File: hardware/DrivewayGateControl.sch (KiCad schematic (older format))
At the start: 50 parts, among them J1 serial_header, J2 magnetometer, J3 power, J4 Motor_Connects, J5 gpio1, J6 gpio2, K1 relay1, K2 relay2, K3 relay3, K4 relay4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

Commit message: fixed wildly wrong shunt resistor value
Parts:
- R10, R7: value 100 -> 0.1
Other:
- note added: "3 amps through 0.1ohm shunt resistor is 0.3 watts\n1/2watt minimum resistor recommended\n"
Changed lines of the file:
@@
 P 10790 1760
 F 0 "R10" H 10860 1806 50  0000 L CNN
-F 1 "100" H 10860 1715 50  0000 L CNN
+F 1 "0.1" H 10860 1715 50  0000 L CNN
 F 2 "Resistor_THT:R_Axial_DIN0207_L6.3mm_D2.5mm_P10.16mm_Horizontal" V 10720 1760 50  0001 C CNN
 F 3 "~" H 10790 1760 50  0001 C CNN
@@
 P 8180 1730
 F 0 "R7" H 8250 1776 50  0000 L CNN
-F 1 "100" H 8250 1685 50  0000 L CNN
+F 1 "0.1" H 8250 1685 50  0000 L CNN
 F 2 "Resistor_THT:R_Axial_DIN0207_L6.3mm_D2.5mm_P10.16mm_Horizontal" V 8110 1730 50  0001 C CNN
 F 3 "~" H 8180 1730 50  0001 C CNN
@@
 	0    -1   -1   0
 $EndComp
+Text Notes 11325 1830 0    50   ~ 0
+3 amps through 0.1ohm shunt resistor is 0.3 watts\n1/2watt minimum resistor recommended\n
 $EndSCHEMATC

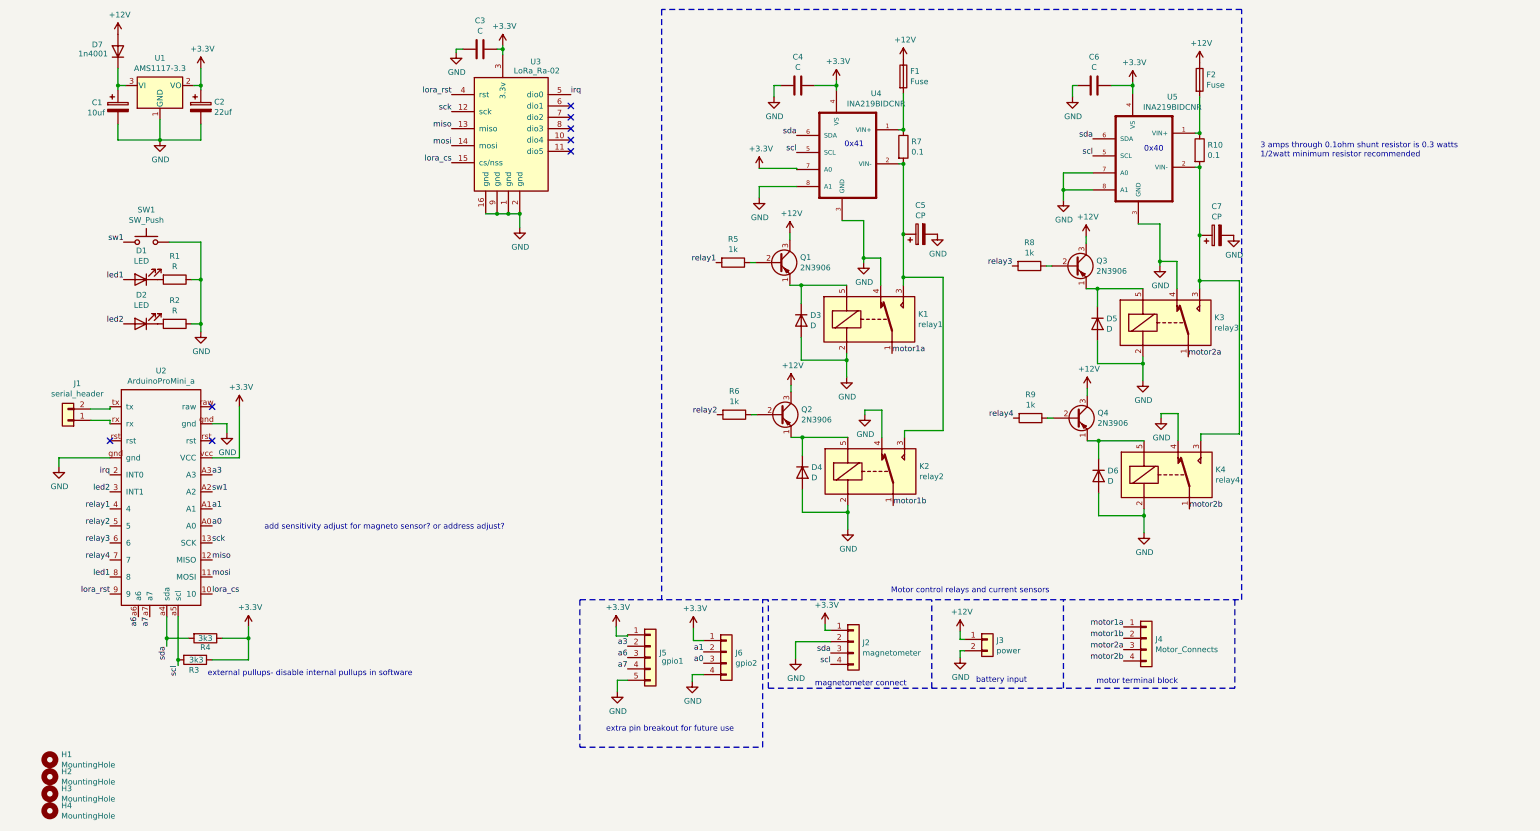
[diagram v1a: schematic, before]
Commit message: update silkscreen, add more pin breakouts
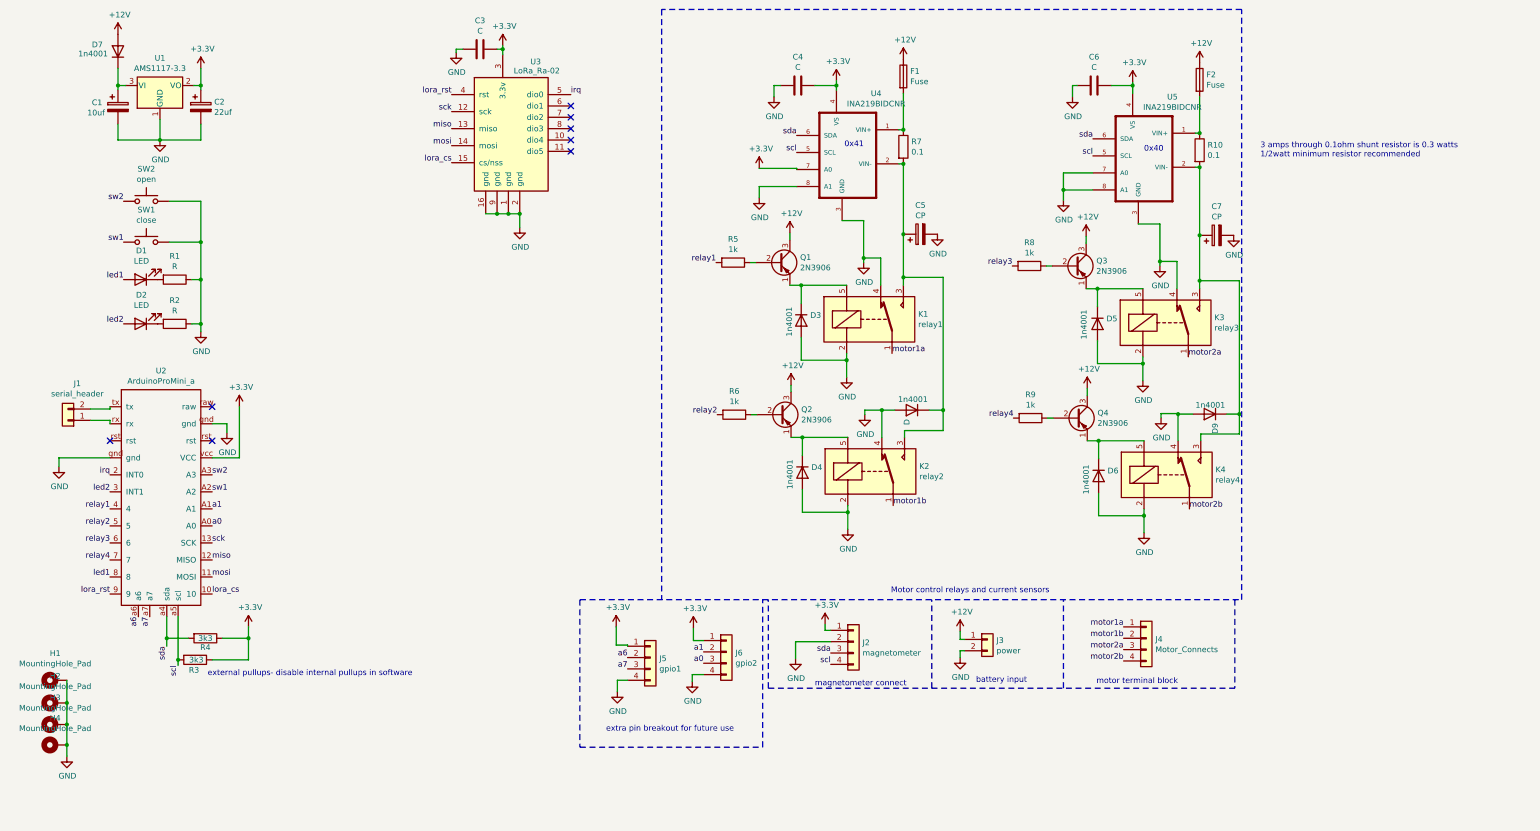
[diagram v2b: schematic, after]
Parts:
- removed H1, H2, H3, H4: MountingHole, MountingHole:MountingHole_3.2mm_M3_Pad_Via, symbol Mechanical:MountingHole
- removed J5: gpio1, Connector_PinHeader_2.54mm:PinHeader_1x05_P2.54mm_Vertical, symbol Connector_Generic:Conn_01x05
- added 1n4001: D, Diode_THT:D_A-405_P7.62mm_Horizontal, symbol Device:D
- added D9: 1n4001, Diode_THT:D_A-405_P7.62mm_Horizontal, symbol Device:D
- added H1, H2, H3, H4: MountingHole_Pad, MountingHole:MountingHole_3.2mm_M3_Pad_Via, symbol Mechanical:MountingHole_Pad
- added J5: gpio1, Connector_PinHeader_2.54mm:PinHeader_1x04_P2.54mm_Vertical, symbol Connector_Generic:Conn_01x04
- added SW2: open, Button_Switch_THT:SW_PUSH_6mm_H8.5mm, symbol Switch:SW_Push
- D3, D4, D5, D6: value D -> 1n4001
- SW1: value SW_Push -> close
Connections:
- net +3V3: now also J5.1 (Pin_1)
- net GND: now also 1n4001.2 (A), D9.2 (A), H1.1, H2.1, H3.1, H4.1, J5.4 (Pin_4), SW2.2
- net a6: now also J5.2 (Pin_2)
- net a7: now also J5.3 (Pin_3)
- net at C7.1, K3.3, K4.3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: now also D9.1 (K)
- net at C5.1, K1.3, K2.3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: now also 1n4001.1 (K)
- net a3 renamed sw2
- net sw2: now also SW2.1
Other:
- note removed: "add sensitivity adjust for magneto sensor? or address adjust?"
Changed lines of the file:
@@
-$EndComp
-$Comp
-L Device:D D5
-U 1 1 5D1CEA1D
-P 9890 3290
-F 0 "D5" V 9844 3369 50  0000 L CNN
-F 1 "D" V 9935 3369 50  0000 L CNN
-F 2 "Diode_THT:D_A-405_P7.62mm_Horizontal" H 9890 3290 50  0001 C CNN
-F 3 "~" H 9890 3290 50  0001 C CNN
-	1    9890 3290
-	0    1    1    0
 $EndComp
 $Comp
@@
 $EndComp
 $Comp
-L Device:D D6
-U 1 1 5D1F4864
-P 9900 4630
-F 0 "D6" V 9854 4709 50  0000 L CNN
-F 1 "D" V 9945 4709 50  0000 L CNN
-F 2 "Diode_THT:D_A-405_P7.62mm_Horizontal" H 9900 4630 50  0001 C CNN
-F 3 "~" H 9900 4630 50  0001 C CNN
-	1    9900 4630
-	0    1    1    0
-$EndComp
-$Comp
 L Device:R R9
 U 1 1 5D1F4878
@@
 	10450 4080 10600 4080
 Wire Wire Line
-	10600 4080 10600 4320
+	10600 4080 10600 4085
 $Comp
 L power:GND #PWR0109
@@
 	10800 4260 11140 4260
 Wire Wire Line
-	11140 4260 11140 2910
+	11140 4260 11140 4085
 Wire Wire Line
 	11140 2910 10790 2910
@@
 $EndComp
 $Comp
-L Device:D D3
-U 1 1 5D30AF9E
-P 7280 3260
-F 0 "D3" V 7234 3339 50  0000 L CNN
-F 1 "D" V 7325 3339 50  0000 L CNN
-F 2 "Diode_THT:D_A-405_P7.62mm_Horizontal" H 7280 3260 50  0001 C CNN
-F 3 "~" H 7280 3260 50  0001 C CNN
-	1    7280 3260
-	0    1    1    0
-$EndComp
-$Comp
 L Device:R R5
 U 1 1 5D30AFB2
@@
 $EndComp
 $Comp
-L Device:D D4
-U 1 1 5D30AFFC
-P 7290 4600
-F 0 "D4" V 7244 4679 50  0000 L CNN
-F 1 "D" V 7335 4679 50  0000 L CNN
-F 2 "Diode_THT:D_A-405_P7.62mm_Horizontal" H 7290 4600 50  0001 C CNN
-F 3 "~" H 7290 4600 50  0001 C CNN
-	1    7290 4600
-	0    1    1    0
-$EndComp
-$Comp
 L Device:R R6
 U 1 1 5D30B010
@@
 	8190 4230 8530 4230
 Wire Wire Line
-	8530 4230 8530 2880
+	8530 4230 8530 4050
 Wire Wire Line
 	8530 2880 8180 2880
@@
 P 1510 2570
 F 0 "SW1" H 1510 2855 50  0000 C CNN
-F 1 "SW_Push" H 1510 2764 50  0000 C CNN
+F 1 "close" H 1510 2764 50  0000 C CNN
 F 2 "Button_Switch_THT:SW_PUSH_6mm_H8.5mm" H 1510 2770 50  0001 C CNN
 F 3 "~" H 1510 2770 50  0001 C CNN
@@
 	1    0    0    -1
 $EndComp
-Text Notes 2550 5110 0    50   ~ 0
-add sensitivity adjust for magneto sensor? or address adjust?
 $Comp
 L Connector_Generic:Conn_01x04 J2
@@
 Text Notes 10300 1780 0    50   ~ 0
 0x40\n
-$Comp
-L Mechanical:MountingHole H1
-U 1 1 5D1AEA67
-P 660 7130
-F 0 "H1" H 760 7176 50  0000 L CNN
-F 1 "MountingHole" H 760 7085 50  0000 L CNN
-F 2 "MountingHole:MountingHole_3.2mm_M3_Pad_Via" H 660 7130 50  0001 C CNN
-F 3 "~" H 660 7130 50  0001 C CNN
-	1    660  7130
-	1    0    0    -1
-$EndComp
-$Comp
-L Mechanical:MountingHole H2
-U 1 1 5D1AF435
-P 660 7280
-F 0 "H2" H 760 7326 50  0000 L CNN
-F 1 "MountingHole" H 760 7235 50  0000 L CNN
-F 2 "MountingHole:MountingHole_3.2mm_M3_Pad_Via" H 660 7280 50  0001 C CNN
-F 3 "~" H 660 7280 50  0001 C CNN
-	1    660  7280
-	1    0    0    -1
-$EndComp
-$Comp
-L Mechanical:MountingHole H3
-U 1 1 5D1AFC52
-P 660 7430
-F 0 "H3" H 760 7476 50  0000 L CNN
-F 1 "MountingHole" H 760 7385 50  0000 L CNN
-F 2 "MountingHole:MountingHole_3.2mm_M3_Pad_Via" H 660 7430 50  0001 C CNN
-F 3 "~" H 660 7430 50  0001 C CNN
-	1    660  7430
-	1    0    0    -1
-$EndComp
-$Comp
-L Mechanical:MountingHole H4
-U 1 1 5D1B04B2
-P 660 7580
-F 0 "H4" H 760 7626 50  0000 L CNN
-F 1 "MountingHole" H 760 7535 50  0000 L CNN
-F 2 "MountingHole:MountingHole_3.2mm_M3_Pad_Via" H 660 7580 50  0001 C CNN
-F 3 "~" H 660 7580 50  0001 C CNN
-	1    660  7580
-	1    0    0    -1
-$EndComp
 Text Notes 2050 6400 0    50   ~ 0
 external pullups- disable internal pullups in software
@@
 Text Label 1540 5870 3    50   ~ 0
 a7
-Text Label 2090 4620 0    50   ~ 0
-a3
 Text Label 2090 5070 0    50   ~ 0
 a0
@@
 Text Label 6420 6280 2    50   ~ 0
 a0
-Text Label 5750 6130 2    50   ~ 0
-a3
 Text Label 5750 6330 2    50   ~ 0
 a7
@@
 	6320 6380 6420 6380
 $Comp
-L Connector_Generic:Conn_01x05 J5
-U 1 1 5D263641
-P 5950 6230
-F 0 "J5" H 6030 6272 50  0000 L CNN
-F 1 "gpio1" H 6050 6200 50  0000 L CNN
-F 2 "Connector_PinHeader_2.54mm:PinHeader_1x05_P2.54mm_Vertical" H 5950 6230 50  0001 C CNN
-F 3 "~" H 5950 6230 50  0001 C CNN
-	1    5950 6230
-	1    0    0    -1
-$EndComp
-$Comp
 L power:+3.3V #PWR0141
 U 1 1 5D26EAC0
@@
 	5660 6430 5660 6530
 Wire Wire Line
-	5650 5960 5650 6040
-Wire Wire Line
-	5650 6040 5750 6040
-Wire Wire Line
-	5750 6040 5750 6030
+	5650 5960 5650 6120
+Wire Wire Line
+	5650 6120 5750 6120
+Wire Wire Line
+	5750 6120 5750 6130
 $Comp
 L Device:D D7
@@
 Text Notes 11325 1830 0    50   ~ 0
 3 amps through 0.1ohm shunt resistor is 0.3 watts\n1/2watt minimum resistor recommended\n
+Wire Wire Line
+	11030 4085 11140 4085
+Connection ~ 11140 4085
+Wire Wire Line
+	11140 4085 11140 2910
+Wire Wire Line
+	10730 4085 10600 4085
+Connection ~ 10600 4085
+Wire Wire Line
+	10600 4085 10600 4320
+Wire Wire Line
+	8105 4050 7990 4050
+Connection ~ 7990 4050
+Wire Wire Line
+	8405 4050 8530 4050
+Connection ~ 8530 4050
+Wire Wire Line
+	8530 4050 8530 2880
+$Comp
+L Device:D 1n4001
+U 1 1 5D254DFC
+P 8255 4050
+F 0 "1n4001" H 8115 3955 50  0000 L CNN
+F 1 "D" V 8300 4129 50  0000 L CNN
+F 2 "Diode_THT:D_A-405_P7.62mm_Horizontal" H 8255 4050 50  0001 C CNN
+F 3 "~" H 8255 4050 50  0001 C CNN
+	1    8255 4050
+	-1   0    0    1
+$EndComp
+$Comp
+L Device:D D5
+U 1 1 5D1CEA1D
+P 9890 3290
+F 0 "D5" V 9844 3369 50  0000 L CNN
+F 1 "1n4001" H 9765 3170 50  0000 L CNN
+F 2 "Diode_THT:D_A-405_P7.62mm_Horizontal" H 9890 3290 50  0001 C CNN
+F 3 "~" H 9890 3290 50  0001 C CNN
+	1    9890 3290
+	0    1    1    0
+$EndComp
+$Comp
+L Device:D D3
+U 1 1 5D30AF9E
+P 7280 3260
+F 0 "D3" V 7234 3339 50  0000 L CNN
+F 1 "1n4001" H 7160 3155 50  0000 L CNN
+F 2 "Diode_THT:D_A-405_P7.62mm_Horizontal" H 7280 3260 50  0001 C CNN
+F 3 "~" H 7280 3260 50  0001 C CNN
+	1    7280 3260
+	0    1    1    0
+$EndComp
+$Comp
+L Device:D D9
+U 1 1 5D255799
+P 10880 4085
+F 0 "D9" V 10834 4164 50  0000 L CNN
+F 1 "1n4001" H 10745 4005 50  0000 L CNN
+F 2 "Diode_THT:D_A-405_P7.62mm_Horizontal" H 10880 4085 50  0001 C CNN
+F 3 "~" H 10880 4085 50  0001 C CNN
+	1    10880 4085
+	-1   0    0    1
+$EndComp
+$Comp
+L Device:D D6
+U 1 1 5D1F4864
+P 9900 4630
+F 0 "D6" V 9854 4709 50  0000 L CNN
+F 1 "1n4001" H 9800 4520 50  0000 L CNN
+F 2 "Diode_THT:D_A-405_P7.62mm_Horizontal" H 9900 4630 50  0001 C CNN
+F 3 "~" H 9900 4630 50  0001 C CNN
+	1    9900 4630
+	0    1    1    0
+$EndComp
+$Comp
+L Device:D D4
+U 1 1 5D30AFFC
+P 7290 4600
+F 0 "D4" V 7244 4679 50  0000 L CNN
+F 1 "1n4001" H 7175 4490 50  0000 L CNN
+F 2 "Diode_THT:D_A-405_P7.62mm_Horizontal" H 7290 4600 50  0001 C CNN
+F 3 "~" H 7290 4600 50  0001 C CNN
+	1    7290 4600
+	0    1    1    0
+$EndComp
+$Comp
+L Switch:SW_Push SW2
+U 1 1 5D2C21C6
+P 1510 2210
+F 0 "SW2" H 1510 2495 50  0000 C CNN
+F 1 "open" H 1510 2404 50  0000 C CNN
+F 2 "Button_Switch_THT:SW_PUSH_6mm_H8.5mm" H 1510 2410 50  0001 C CNN
+F 3 "~" H 1510 2410 50  0001 C CNN
+	1    1510 2210
+	1    0    0    -1
+$EndComp
+Wire Wire Line
+	1710 2210 1990 2210
+Wire Wire Line
+	1990 2210 1990 2570
+Connection ~ 1990 2570
+Text Label 1310 2210 2    50   ~ 0
+sw2
+Text Label 2090 4620 0    50   ~ 0
+sw2
+$Comp
+L Connector_Generic:Conn_01x04 J5
+U 1 1 5D2CF3C3
+P 5950 6230
+F 0 "J5" H 6030 6222 50  0000 L CNN
+F 1 "gpio1" H 6030 6131 50  0000 L CNN
+F 2 "Connector_PinHeader_2.54mm:PinHeader_1x04_P2.54mm_Vertical" H 5950 6230 50  0001 C CNN
+F 3 "~" H 5950 6230 50  0001 C CNN
+	1    5950 6230
+	1    0    0    -1
+$EndComp
+$Comp
+L Mechanical:MountingHole_Pad H2
+U 1 1 5D2F3DBA
+P 710 6630
+F 0 "H2" V 947 6633 50  0000 C CNN
+F 1 "MountingHole_Pad" V 856 6633 50  0000 C CNN
+F 2 "MountingHole:MountingHole_3.2mm_M3_Pad_Via" H 710 6630 50  0001 C CNN
+F 3 "~" H 710 6630 50  0001 C CNN
+	1    710  6630
+	0    -1   -1   0
+$EndComp
+$Comp
+L Mechanical:MountingHole_Pad H1
+U 1 1 5D2F4284
+P 710 6430
+F 0 "H1" V 947 6433 50  0000 C CNN
+F 1 "MountingHole_Pad" V 856 6433 50  0000 C CNN
+F 2 "MountingHole:MountingHole_3.2mm_M3_Pad_Via" H 710 6430 50  0001 C CNN
+F 3 "~" H 710 6430 50  0001 C CNN
+	1    710  6430
+	0    -1   -1   0
+$EndComp
+$Comp
+L Mechanical:MountingHole_Pad H3
+U 1 1 5D3143F9
+P 710 6820
+F 0 "H3" V 947 6823 50  0000 C CNN
+F 1 "MountingHole_Pad" V 856 6823 50  0000 C CNN
+F 2 "MountingHole:MountingHole_3.2mm_M3_Pad_Via" H 710 6820 50  0001 C CNN
+F 3 "~" H 710 6820 50  0001 C CNN
+	1    710  6820
+	0    -1   -1   0
+$EndComp
+$Comp
+L Mechanical:MountingHole_Pad H4
+U 1 1 5D314874
+P 710 7000
+F 0 "H4" V 947 7003 50  0000 C CNN
+F 1 "MountingHole_Pad" V 856 7003 50  0000 C CNN
+F 2 "MountingHole:MountingHole_3.2mm_M3_Pad_Via" H 710 7000 50  0001 C CNN
+F 3 "~" H 710 7000 50  0001 C CNN
+	1    710  7000
+	0    -1   -1   0
+$EndComp
+Wire Wire Line
+	810  6430 810  6630
+Connection ~ 810  6630
+Wire Wire Line
+	810  6630 810  6820
+Connection ~ 810  6820
+Wire Wire Line
+	810  6820 810  7000
+Connection ~ 810  7000
+Wire Wire Line
+	810  7000 810  7100
+$Comp
+L power:GND #PWR0143
+U 1 1 5D31DB8C
+P 810 7100
+F 0 "#PWR0143" H 810 6850 50  0001 C CNN
+F 1 "GND" H 815 6927 50  0000 C CNN
+F 2 "" H 810 7100 50  0001 C CNN
+F 3 "" H 810 7100 50  0001 C CNN
+	1    810  7100
+	1    0    0    -1
+$EndComp
 $EndSCHEMATC

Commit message: fixed relay switch issue
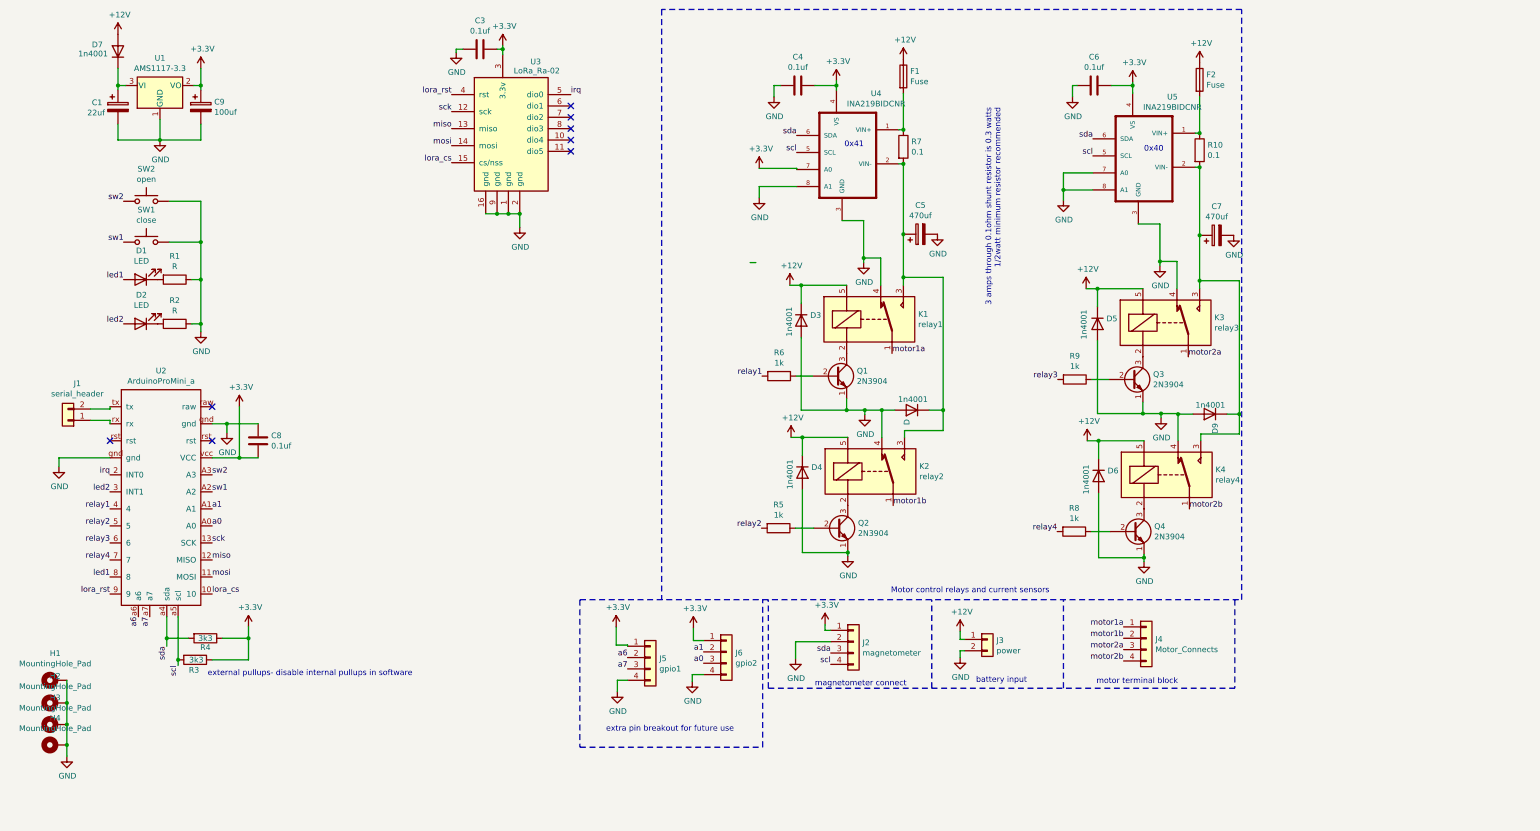
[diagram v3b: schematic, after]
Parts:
- removed C2: 22uf, Capacitor_THT:CP_Radial_D5.0mm_P2.50mm, symbol Device:CP
- removed Q1, Q2, Q3, Q4: 2N3906, Package_TO_SOT_THT:TO-92_Inline_Wide, symbol Transistor_BJT:2N3906
- added C8: 0.1uf, Capacitor_THT:C_Disc_D4.7mm_W2.5mm_P5.00mm, symbol Device:C
- added C9: 100uf, Capacitor_THT:CP_Radial_D7.5mm_P2.50mm, symbol Device:CP
- added Q1, Q2, Q3, Q4: 2N3904, Package_TO_SOT_THT:TO-92_Inline_Wide, symbol Transistor_BJT:2N3904
- C1: value 10uf -> 22uf
- C3, C4, C6: value C -> 0.1uf
- C5, C7: value CP -> 470uf; footprint Capacitor_THT:CP_Radial_D10.0mm_P5.00mm -> Capacitor_THT:CP_Radial_D12.5mm_P5.00mm
- R1, R2, R3, R4, R5, R6, R8, R9: footprint Resistor_THT:R_Axial_DIN0204_L3.6mm_D1.6mm_P5.08mm_Horizontal -> Resistor_THT:R_Axial_DIN0207_L6.3mm_D2.5mm_P7.62mm_Horizontal
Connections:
- net +12V: now also D3.1 (K), D4.1 (K), D5.1 (K), D6.1 (K), K1.5, K2.5, K3.5, K4.5
- net +3V3: now also C8.2, C9.1
- net GND: now also C8.1, C9.2, Q1.1 (E), Q2.1 (E), Q3.1 (E), Q4.1 (E); no longer K1.2, K2.2, K3.2, K4.2
- net relay1: now also R6.2; no longer R5.2
- net relay2: now also R5.2; no longer R6.2
- net relay3: now also R9.2; no longer R8.2
- net relay4: now also R8.2; no longer R9.2
- net at R5.1: now also Q2.2 (B)
- net at R6.1: now also Q1.2 (B)
- net at R9.1: now also Q3.2 (B)
- net at R8.1: now also Q4.2 (B)
- new net: K3.2, Q3.3 (C)
- new net: K4.2, Q4.3 (C)
- new net: K1.2, Q1.3 (C)
- new net: K2.2, Q2.3 (C)
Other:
- moved on the sheet: R5, R6, R8, R9
